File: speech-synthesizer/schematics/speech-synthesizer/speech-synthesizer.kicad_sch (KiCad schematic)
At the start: 12 parts

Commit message: tweaks and improvements
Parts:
- added R?: 1M, symbol Device:R
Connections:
- net GND: now also R?.1
- net IRST: now reaches U?.15 (I/O1)
- net IRST: now also R?.2
- no-connect marks 16 -> 15
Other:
- moved on the sheet: C?, R?, U?

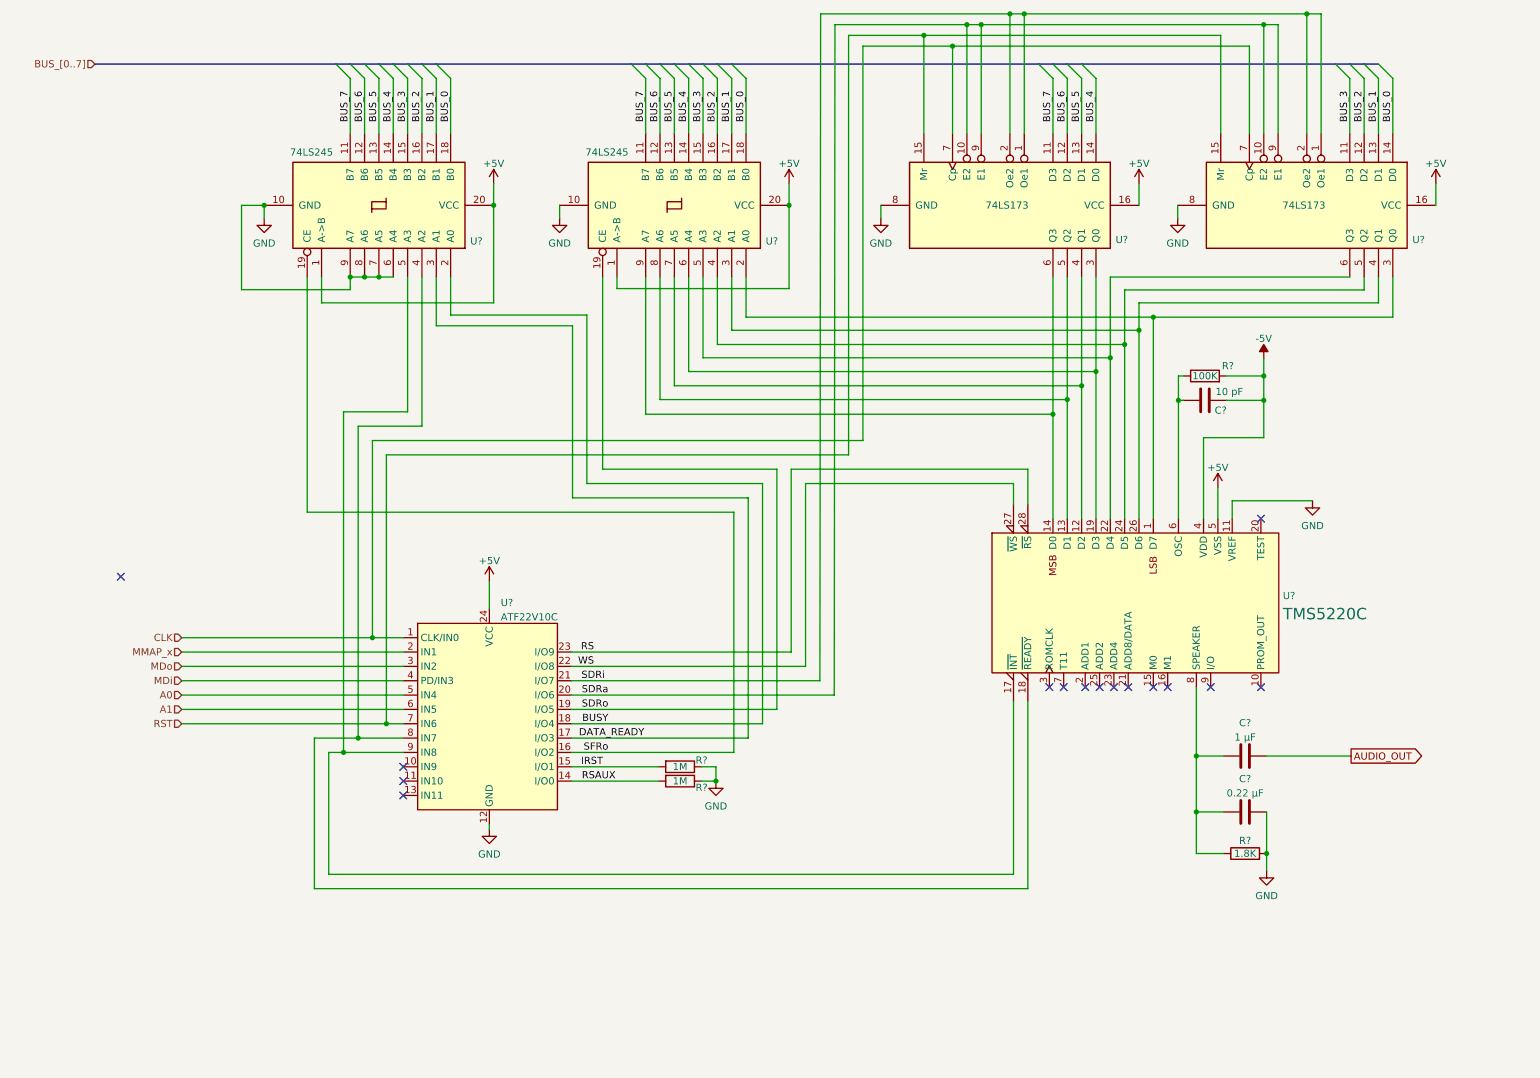
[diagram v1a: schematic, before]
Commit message: reworked design of speech module
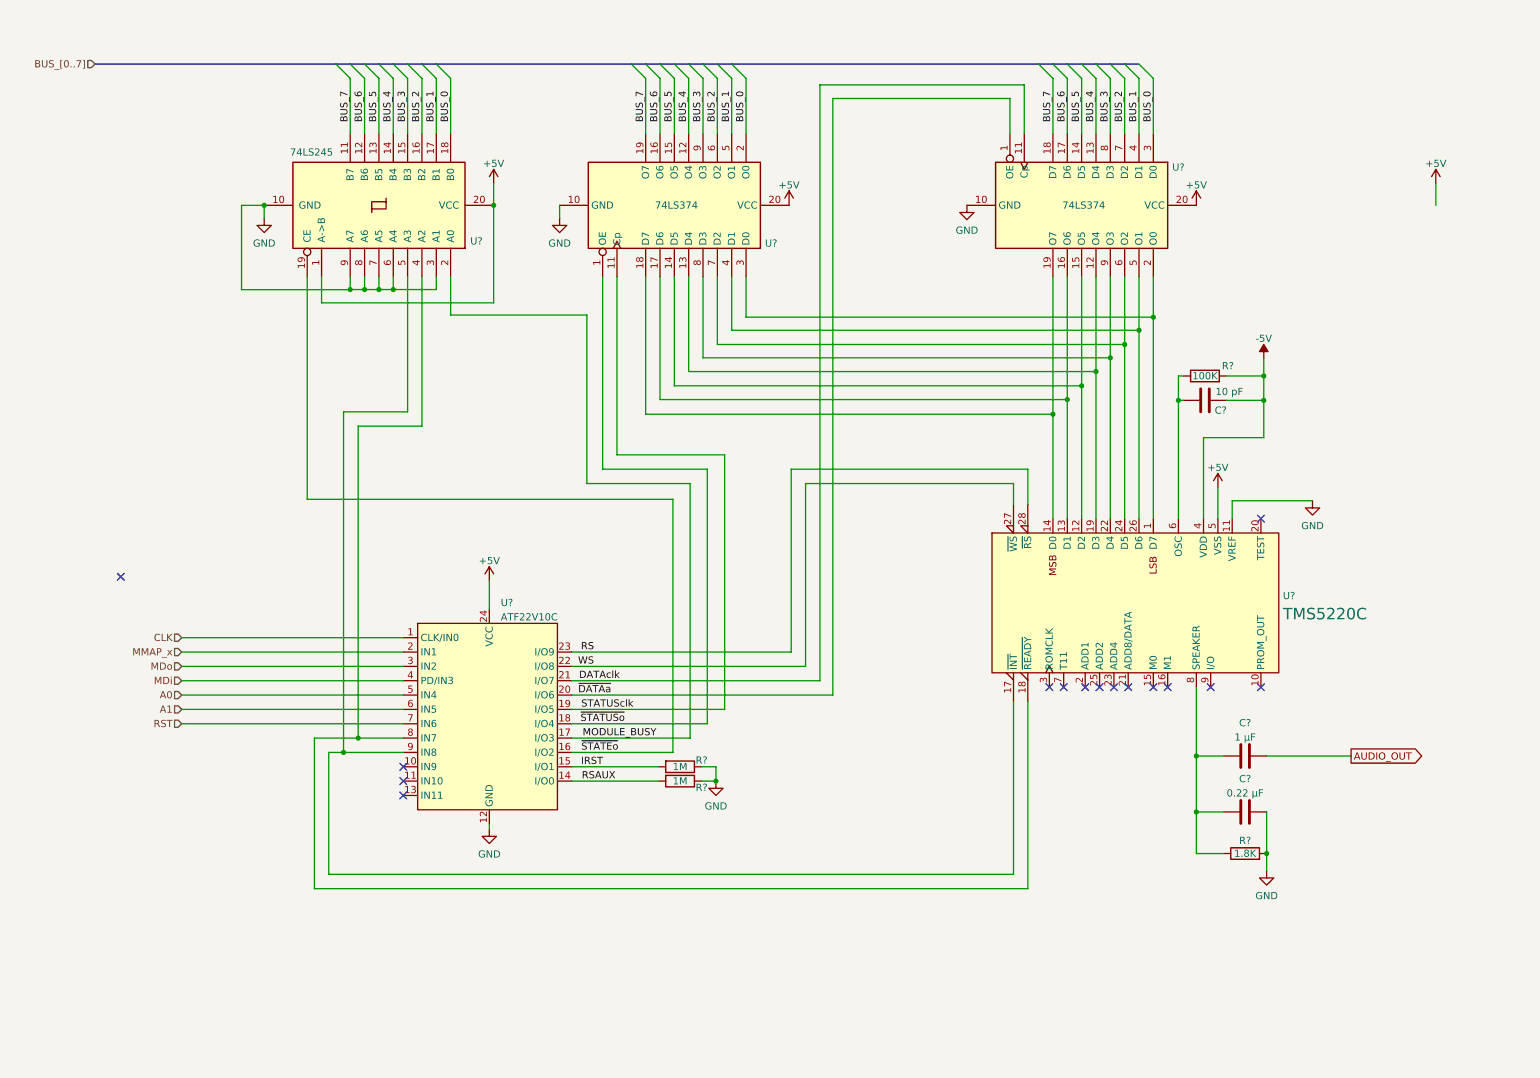
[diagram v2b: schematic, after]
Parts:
- removed U? (x2): 74LS173, symbol 74xx:74LS173
- removed U?: 74LS245, symbol 74xx:74LS245
- added U? (x2): 74LS374, symbol 74xx:74LS374
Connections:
- net +5V: now also U?.20 (VCC), U?.20 (VCC)
- net BUS_0: now also U?.2 (O0), U?.3 (D0)
- net BUS_1: now also U?.4 (D1), U?.5 (O1)
- net BUS_2: now also U?.6 (O2), U?.7 (D2)
- net BUS_3: now also U?.8 (D3), U?.9 (O3)
- net BUS_4: now also U?.12 (O4), U?.13 (D4)
- net BUS_5: now also U?.14 (D5), U?.15 (O5)
- net BUS_6: now also U?.16 (O6), U?.17 (D6)
- net BUS_7: now also U?.18 (D7), U?.19 (O7)
- net GND: now also U?.3 (A1), U?.10 (GND), U?.10 (GND)
- net at U?.1 (D7): now also U?.2 (O0), U?.3 (D0)
- net at U?.26 (D6): now also U?.4 (D1), U?.5 (O1)
- net at U?.24 (D5): now also U?.6 (O2), U?.7 (D2)
- net at U?.22 (D4): now also U?.8 (D3), U?.9 (O3)
- net at U?.19 (D3): now also U?.12 (O4), U?.13 (D4)
- net at U?.12 (D2): now also U?.14 (D5), U?.15 (O5)
- net at U?.13 (D1): now also U?.16 (O6), U?.17 (D6)
- net at U?.14 (D0): now also U?.18 (D7), U?.19 (O7)
- net BUSY renamed MODULE_BUSY
- net MODULE_BUSY: now also U?.17 (I/O3); no longer U?.18 (I/O4)
- removed net DATA_READY: U?.17 (I/O3), U?.3 (A1)
- net SDRa renamed ~{DATAa}
- net ~{DATAa}: now also U?.1 (OE)
- net SDRi renamed DATAclk
- net DATAclk: now also U?.11 (Cp)
- net SDRo renamed STATUSclk
- net STATUSclk: now also U?.11 (Cp)
- net SFRo renamed ~{STATEo}
- new net ~{STATUSo}: U?.1 (OE), U?.18 (I/O4)

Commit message: first update to pld
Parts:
- removed R? (x2): 1M, symbol Device:R
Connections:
- net GND: now also U?.13 (IN11)
- net MODULE_BUSY: now also U?.16 (I/O2); no longer U?.17 (I/O3)
- net ~{STATEo}: now also U?.17 (I/O3); no longer U?.16 (I/O2)
- net DATAclk renamed DATAi
- net IRST: no longer names the net of U?.15 (I/O1)
- net RSAUX: no longer names the net of U?.14 (I/O0)
- net STATUSclk renamed STATUSi
- no-connect marks 15 -> 14
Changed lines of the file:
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@@
   (junction (at 203.073 77.7043) (diameter 0) (color 0 0 0 0)
-  )
-  (junction (at 135.763 150.241) (diameter 0) (color 0 0 0 0)
   )
   (junction (at 233.299 163.068) (diameter 0) (color 0 0 0 0)
@@
   (no_connect (at 80.391 147.701))
   (no_connect (at 80.391 150.241))
-  (no_connect (at 80.391 152.781))
   (no_connect (at 201.168 133.604))
   (no_connect (at 203.708 133.604))
@@
     (stroke (width 0) (type default) (color 0 0 0 0))
   )
-  (wire (pts (xy 110.236 150.241) (xy 125.603 150.241))
-    (stroke (width 0) (type default) (color 0 0 0 0))
-  )
   (wire (pts (xy 69.8073 84.836) (xy 81.153 84.836))
     (stroke (width 0) (type default) (color 0 0 0 0))
@@
     (stroke (width 0) (type default) (color 0 0 0 0))
   )
+  (wire (pts (xy 71.501 152.781) (xy 80.391 152.781))
+    (stroke (width 0) (type default) (color 0 0 0 0))
+  )
   (wire (pts (xy 76.073 63.1768) (xy 76.073 60.96))
     (stroke (width 0) (type default) (color 0 0 0 0))
@@
     (stroke (width 0) (type default) (color 0 0 0 0))
   )
-  (wire (pts (xy 131.191 142.621) (xy 110.236 142.621))
+  (wire (pts (xy 131.191 145.161) (xy 110.236 145.161))
     (stroke (width 0) (type default) (color 0 0 0 0))
   )
@@
     (stroke (width 0) (type default) (color 0 0 0 0))
   )
-  (wire (pts (xy 110.236 145.161) (xy 128.143 145.161))
-    (stroke (width 0) (type default) (color 0 0 0 0))
-  )
-  (wire (pts (xy 135.763 147.701) (xy 135.763 150.241))
+  (wire (pts (xy 110.236 142.621) (xy 128.143 142.621))
     (stroke (width 0) (type default) (color 0 0 0 0))
   )
@@
     (stroke (width 0) (type default) (color 0 0 0 0))
   )
-  (wire (pts (xy 131.191 97.536) (xy 131.191 142.621))
+  (wire (pts (xy 131.191 97.536) (xy 131.191 145.161))
     (stroke (width 0) (type default) (color 0 0 0 0))
   )
@@
     (stroke (width 0) (type default) (color 0 0 0 0))
   )
-  (wire (pts (xy 133.223 150.241) (xy 135.763 150.241))
-    (stroke (width 0) (type default) (color 0 0 0 0))
-  )
   (wire (pts (xy 226.187 78.486) (xy 232.791 78.486))
     (stroke (width 0) (type default) (color 0 0 0 0))
@@
     (stroke (width 0) (type default) (color 0 0 0 0))
   )
-  (wire (pts (xy 110.236 147.701) (xy 125.603 147.701))
-    (stroke (width 0) (type default) (color 0 0 0 0))
-  )
   (wire (pts (xy 115.697 94.996) (xy 134.239 94.996))
     (stroke (width 0) (type default) (color 0 0 0 0))
@@
     (stroke (width 0) (type default) (color 0 0 0 0))
   )
-  (wire (pts (xy 128.143 145.161) (xy 128.143 100.33))
+  (wire (pts (xy 128.143 142.621) (xy 128.143 100.33))
     (stroke (width 0) (type default) (color 0 0 0 0))
   )
@@
     (stroke (width 0) (type default) (color 0 0 0 0))
   )
-  (wire (pts (xy 133.223 147.701) (xy 135.763 147.701))
-    (stroke (width 0) (type default) (color 0 0 0 0))
-  )
   (wire (pts (xy 191.008 136.144) (xy 191.008 169.291))
     (stroke (width 0) (type default) (color 0 0 0 0))
@@
     (stroke (width 0) (type default) (color 0 0 0 0))
   )
-  (label "RSAUX" (at 117.983 150.241 180)
-    (effects (font (size 1.27 1.27)) (justify right bottom))
-  )
   (label "BUS_2" (at 208.153 33.528 90)
     (effects (font (size 1.27 1.27)) (justify left bottom))
@@
     (effects (font (size 1.27 1.27)) (justify left bottom))
   )
+  (label "~{OE}" (at 75.946 152.781 0)
+    (effects (font (size 1.27 1.27)) (justify left bottom))
+  )
   (label "BUS_4" (at 203.073 33.528 90)
     (effects (font (size 1.27 1.27)) (justify left bottom))
   )
-  (label "IRST" (at 111.8694 147.701 0)
-    (effects (font (size 1.27 1.27)) (justify left bottom))
-  )
   (label "BUS_6" (at 125.857 33.528 90)
     (effects (font (size 1.27 1.27)) (justify left bottom))
@@
     (effects (font (size 1.27 1.27)) (justify left bottom))
   )
-  (label "DATAclk" (at 118.745 132.461 180)
+  (label "DATAi" (at 116.586 132.461 180)
     (effects (font (size 1.27 1.27)) (justify right bottom))
   )
@@
     (effects (font (size 1.27 1.27)) (justify left bottom))
   )
-  (label "STATUSclk" (at 121.158 137.541 180)
+  (label "STATUSi" (at 118.999 137.541 180)
     (effects (font (size 1.27 1.27)) (justify right bottom))
   )
@@
     (effects (font (size 1.27 1.27)) (justify left bottom))
   )
-  (label "~{STATEo}" (at 118.491 145.161 180)
+  (label "~{STATEo}" (at 118.491 142.621 180)
     (effects (font (size 1.27 1.27)) (justify right bottom))
   )
@@
     (effects (font (size 1.27 1.27)) (justify left bottom))
   )
-  (label "MODULE_BUSY" (at 125.222 142.621 180)
+  (label "MODULE_BUSY" (at 125.222 145.161 180)
     (effects (font (size 1.27 1.27)) (justify right bottom))
   )
@@
     (pin "9")
   )
-  (symbol (lib_id "Device:R") (at 129.413 147.701 270) (unit 1)
-    (in_bom yes) (on_board yes)
-    (property "Reference" "R?" (id 0) (at 133.223 146.558 90))
-    (property "Value" "1M" (id 1) (at 129.413 147.701 90))
-    (property "Footprint" "" (id 2) (at 129.413 145.923 90)
-      (effects (font (size 1.27 1.27)) hide)
-    )
-    (property "Datasheet" "~" (id 3) (at 129.413 147.701 0)
-      (effects (font (size 1.27 1.27)) hide)
-    )
-    (pin "1")
-    (pin "2")
+  (symbol (lib_id "power:GND") (at 71.501 152.781 0) (unit 1)
+    (in_bom yes) (on_board yes) (fields_autoplaced)
+    (property "Reference" "#PWR?" (id 0) (at 71.501 159.131 0)
+      (effects (font (size 1.27 1.27)) hide)
+    )
+    (property "Value" "GND" (id 1) (at 71.501 157.2244 0))
+    (property "Footprint" "" (id 2) (at 71.501 152.781 0)
+      (effects (font (size 1.27 1.27)) hide)
+    )
+    (property "Datasheet" "" (id 3) (at 71.501 152.781 0)
+      (effects (font (size 1.27 1.27)) hide)
+    )
+    (pin "1")
   )
   (symbol (lib_id "power:+5V") (at 95.631 114.808 0) (unit 1)
@@
     (pin "2")
   )
-  (symbol (lib_id "power:GND") (at 135.763 150.241 0) (unit 1)
-    (in_bom yes) (on_board yes) (fields_autoplaced)
-    (property "Reference" "#PWR?" (id 0) (at 135.763 156.591 0)
-      (effects (font (size 1.27 1.27)) hide)
-    )
-    (property "Value" "GND" (id 1) (at 135.763 154.6844 0))
-    (property "Footprint" "" (id 2) (at 135.763 150.241 0)
-      (effects (font (size 1.27 1.27)) hide)
-    )
-    (property "Datasheet" "" (id 3) (at 135.763 150.241 0)
-      (effects (font (size 1.27 1.27)) hide)
-    )
-    (pin "1")
-  )
   (symbol (lib_id "power:GND") (at 180.213 48.26 0) (unit 1)
     (in_bom yes) (on_board yes) (fields_autoplaced)
@@
     (pin "8")
     (pin "9")
-  )
-  (symbol (lib_id "Device:R") (at 129.413 150.241 270) (unit 1)
-    (in_bom yes) (on_board yes)
-    (property "Reference" "R?" (id 0) (at 133.223 151.384 90))
-    (property "Value" "1M" (id 1) (at 129.413 150.241 90))
-    (property "Footprint" "" (id 2) (at 129.413 148.463 90)
-      (effects (font (size 1.27 1.27)) hide)
-    )
-    (property "Datasheet" "~" (id 3) (at 129.413 150.241 0)
-      (effects (font (size 1.27 1.27)) hide)
-    )
-    (pin "1")
-    (pin "2")
   )
   (symbol (lib_id "power:GND") (at 108.077 50.546 0) (unit 1)
@@
       (reference "#PWR?") (unit 1) (value "+5V") (footprint "")
     )
+    (path "/24a34c17-ce5d-42eb-8b00-ac3de54187b1"
+      (reference "#PWR?") (unit 1) (value "GND") (footprint "")
+    )
     (path "/2d3f8bdb-6bdb-42ce-b67d-e066a213cfa1"
       (reference "#PWR?") (unit 1) (value "+5V") (footprint "")
@@
       (reference "#PWR?") (unit 1) (value "+5V") (footprint "")
     )
-    (path "/71f89d7b-13c0-42f0-8714-416e5100fad2"
-      (reference "#PWR?") (unit 1) (value "GND") (footprint "")
-    )
     (path "/85d13639-729d-45b6-9ee2-35c1b4be849e"
       (reference "#PWR?") (unit 1) (value "GND") (footprint "")
@@
       (reference "C?") (unit 1) (value "0.22 µF") (footprint "")
     )
-    (path "/1a4df658-12f3-45f5-9900-311804a8998a"
-      (reference "R?") (unit 1) (value "1M") (footprint "")
-    )
     (path "/4c8624de-33b8-44b9-995d-0810c60b207a"
       (reference "R?") (unit 1) (value "100K") (footprint "")
@@
       (reference "R?") (unit 1) (value "1.8K") (footprint "")
     )
-    (path "/d6262c75-0bdb-4d19-855e-b2f2431af8be"
-      (reference "R?") (unit 1) (value "1M") (footprint "")
-    )
     (path "/1311717c-35fe-41b0-ad8f-751c99efa809"

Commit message: draft speech code
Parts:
- added D? (x2): LED, symbol Device:LED
- added Q? (x2): 2N4403, symbol Device:Q_PNP_EBC
- added R? (x2): 1K, symbol Device:R
- added R? (x2): 220, symbol Device:R
- added RN?: 10K, Resistor_THT:R_Array_SIP9, symbol Device:R_Network08_US
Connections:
- net +5V: now also Q?.1 (E), Q?.1 (E)
- net GND: now also R?.2, R?.2, RN?.1 (common)
- net at U?.18 (~{READY}), U?.4 (A2), U?.8 (IN7): now also R?.2
- net at U?.17 (~{INT}), U?.5 (A3), U?.9 (IN8): now also R?.2
- net at U?.12 (O4), U?.13 (D4), U?.19 (D3): now also RN?.5 (R4)
- net at U?.12 (D2), U?.14 (D5), U?.15 (O5): now also RN?.4 (R3)
- net at U?.13 (D1), U?.16 (O6), U?.17 (D6): now also RN?.3 (R2)
- net at U?.14 (D0), U?.18 (D7), U?.19 (O7): now also RN?.2 (R1)
- net at U?.1 (D7), U?.2 (O0), U?.3 (D0): now also RN?.9 (R8)
- net at U?.26 (D6), U?.4 (D1), U?.5 (O1): now also RN?.8 (R7)
- net at U?.24 (D5), U?.6 (O2), U?.7 (D2): now also RN?.7 (R6)
- net at U?.8 (D3), U?.9 (O3): now also RN?.6 (R5); no longer U?.22 (D4)
- new net: D?.1 (K), R?.1 (x2)
- new net: D?.2 (A), Q?.3 (C) (x2)
- new net: Q?.2 (B), R?.1 (x2)
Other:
- note added: "INT Indicator"
- note added: "READY Indicator"
- moved on the sheet: C?, R?, U?

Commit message: tweaks
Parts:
- added D3: LED, symbol Device:LED
- added R5: 220, symbol Device:R
- gave numbers to parts that had none: 19
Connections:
- net GND: now also R5.2
- new net: D3.1 (K), R5.1
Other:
- note added: "BUSY Indicator"
